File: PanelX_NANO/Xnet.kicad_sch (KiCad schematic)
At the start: 8 parts, among them J301 RJ12, U301 MAX485E

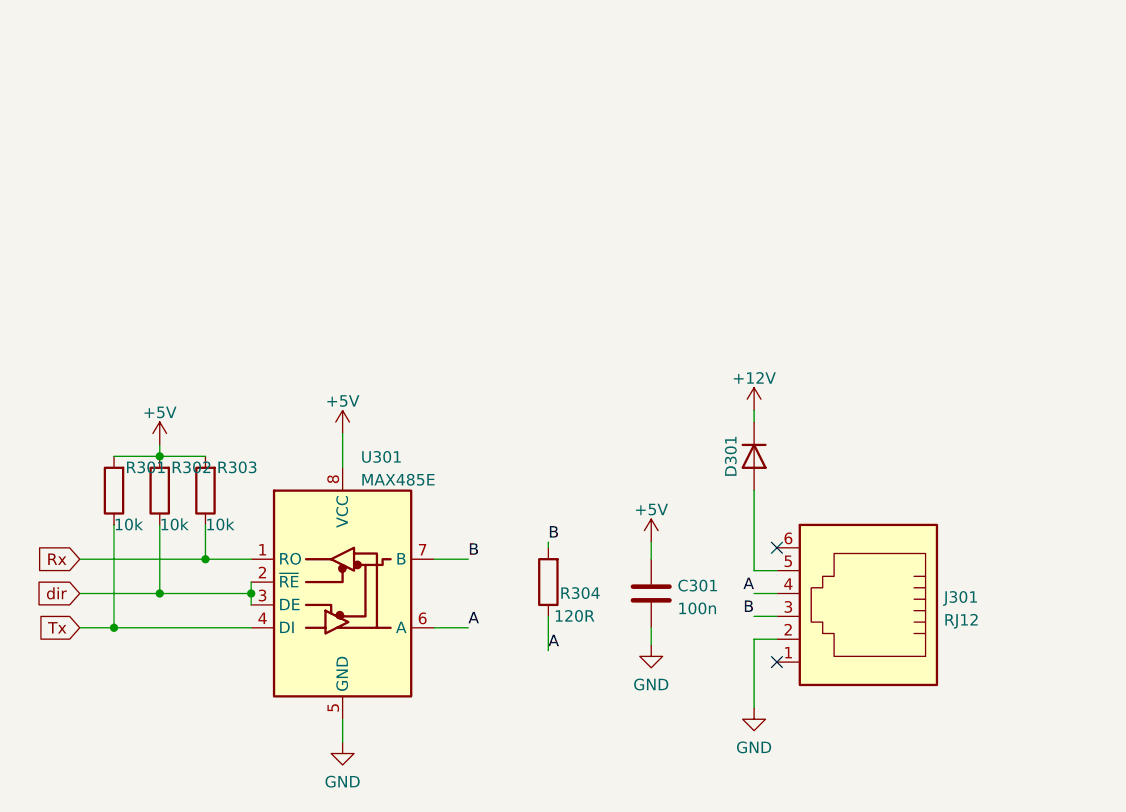
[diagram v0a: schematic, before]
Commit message: added nano project to repo. Must be modular flatcable design. I want to make 2 versions, one with voltage regulator and Xnet and one as I2C slave
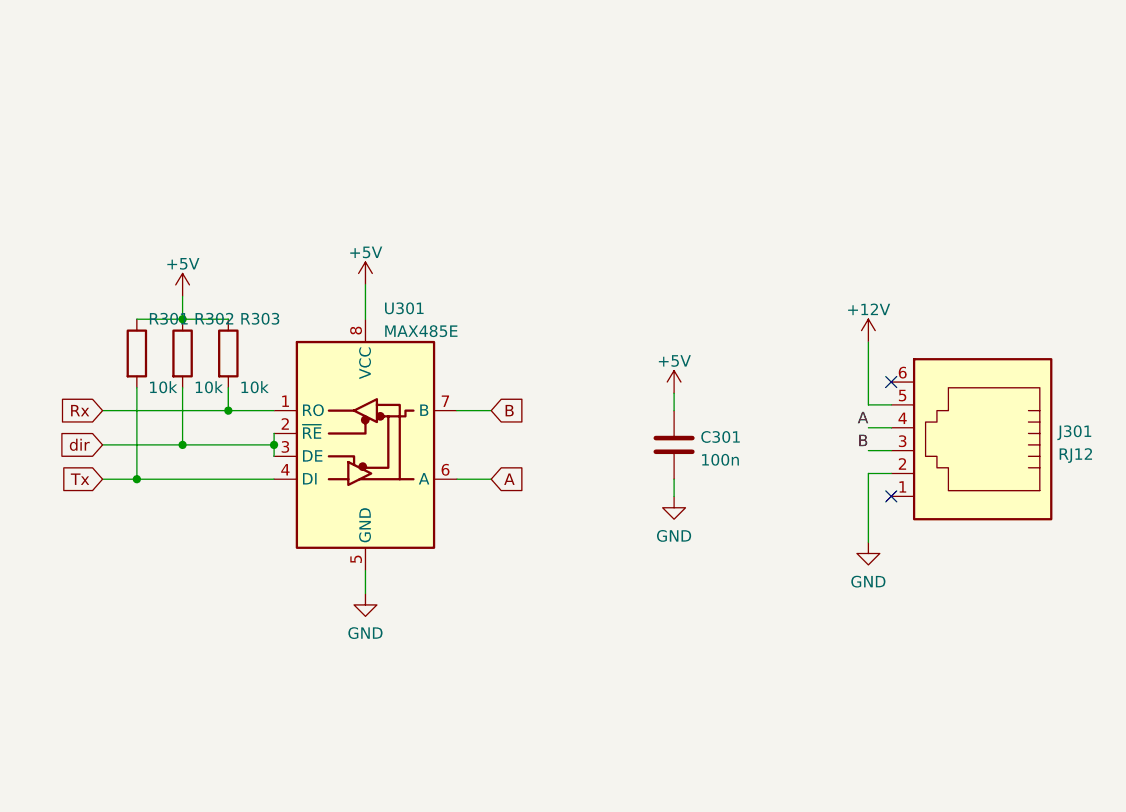
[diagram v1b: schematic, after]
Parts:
- removed D301: D, Diode_SMD:D_SMA, symbol Device:D
- removed R304: 120R, Resistor_SMD:R_0805_2012Metric_Pad1.20x1.40mm_HandSolder, symbol Device:R
- C301: footprint Capacitor_SMD:C_0805_2012Metric_Pad1.18x1.45mm_HandSolder -> Capacitor_SMD:C_0603_1608Metric_Pad1.08x0.95mm_HandSolder; JLCPCB Part# (none) -> C14663
- J301: footprint Connector_RJ:RJ12_Amphenol_54601 -> (none)
- R301, R302, R303: footprint Resistor_SMD:R_0805_2012Metric_Pad1.20x1.40mm_HandSolder -> Resistor_SMD:R_0402_1005Metric; JLCPCB Part# (none) -> C25744
- U301: JLCPCB Part# (none) -> C668206
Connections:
- net +12V: now also J301.5
- net +5V: now also R301.1, R302.1, R303.1; no longer R301.2, R302.2, R303.2
- net Rx: now also R303.2; no longer R303.1
- net Tx: now also R301.2; no longer R301.1
- net dir: now also R302.2; no longer R302.1

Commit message: Deleted zip files from repo
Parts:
- J301: footprint (none) -> Connector_RJ:RJ25_Wayconn_MJEA-660X1_Horizontal
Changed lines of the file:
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@@
       (effects (font (size 1.27 1.27)) (justify right))
     )
-    (property "Footprint" "" (id 2) (at 163.83 72.39 90)
+    (property "Footprint" "Connector_RJ:RJ25_Wayconn_MJEA-660X1_Horizontal" (id 2) (at 163.83 72.39 90)
       (effects (font (size 1.27 1.27)) hide)
     )

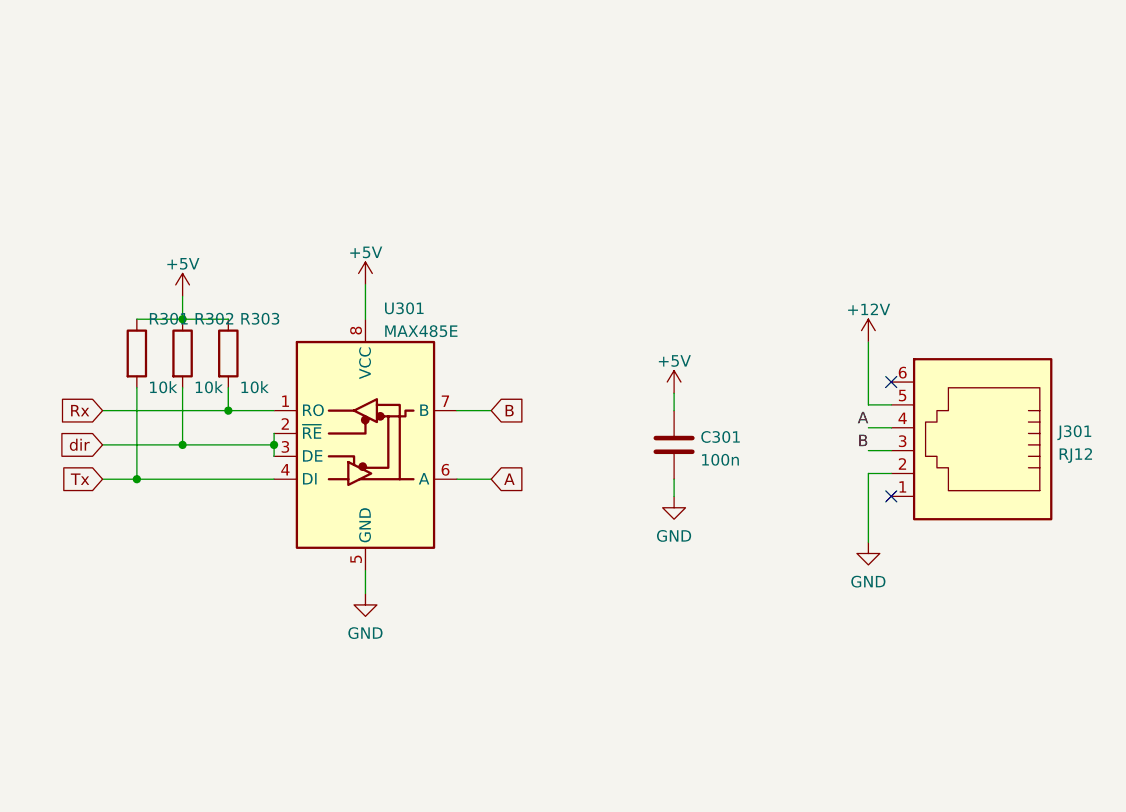
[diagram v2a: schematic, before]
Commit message: I picked a suitable connector. I will use plain 2x12 female n male connectors for the b2b connector. Death to flatcables! The RJ12 connector still goed on the panel carrier board. I will look for vertical SMD variant
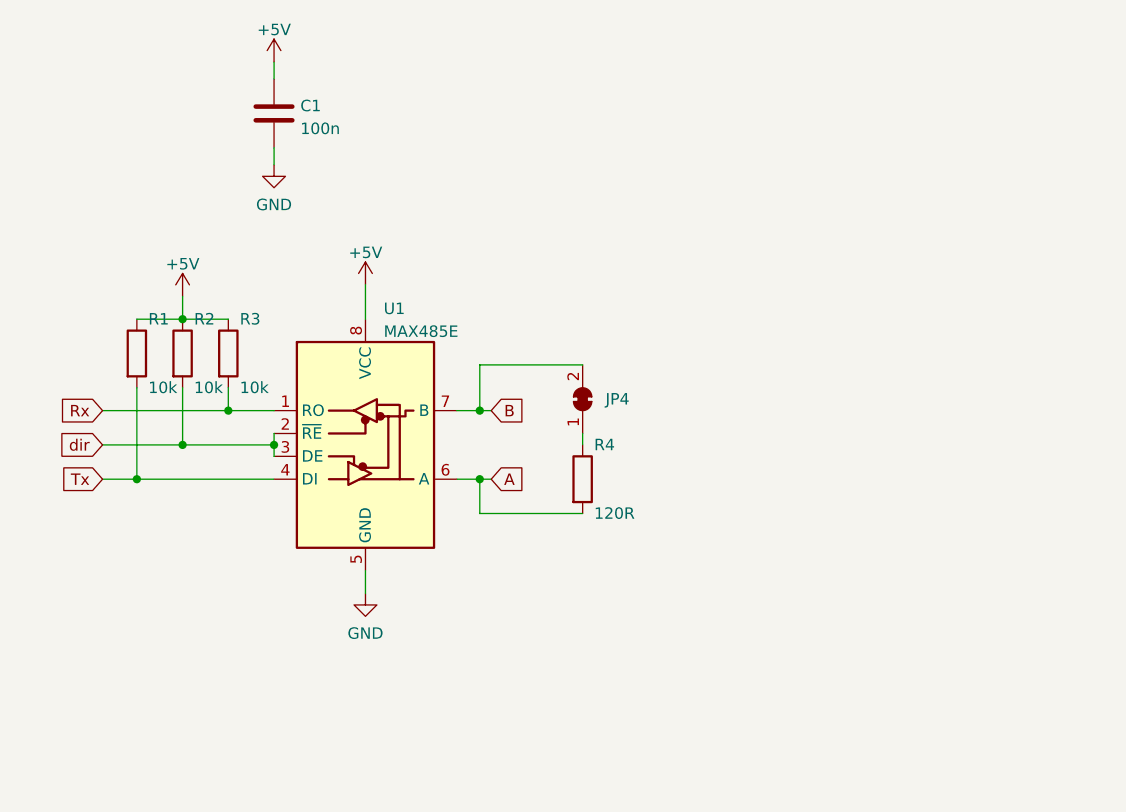
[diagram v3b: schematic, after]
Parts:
- removed J301: RJ12, Connector_RJ:RJ25_Wayconn_MJEA-660X1_Horizontal, symbol Connector:RJ12
- added JP4: SolderJumper_2_Bridged, Jumper:SolderJumper-2_P1.3mm_Bridged_RoundedPad1.0x1.5mm, symbol Jumper:SolderJumper_2_Bridged
- added R4: 120R, Resistor_SMD:R_0402_1005Metric, symbol Device:R
- renumbered C301 to C1, R301 to R1, R302 to R2, R303 to R3, U301 to U1
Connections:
- net A: now also R4.2
- net B: now also JP4.2 (B)
- new net: JP4.1 (A), R4.1
- no-connect marks 2 -> 0
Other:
- moved on the sheet: C1
